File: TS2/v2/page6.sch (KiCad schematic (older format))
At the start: 4 parts

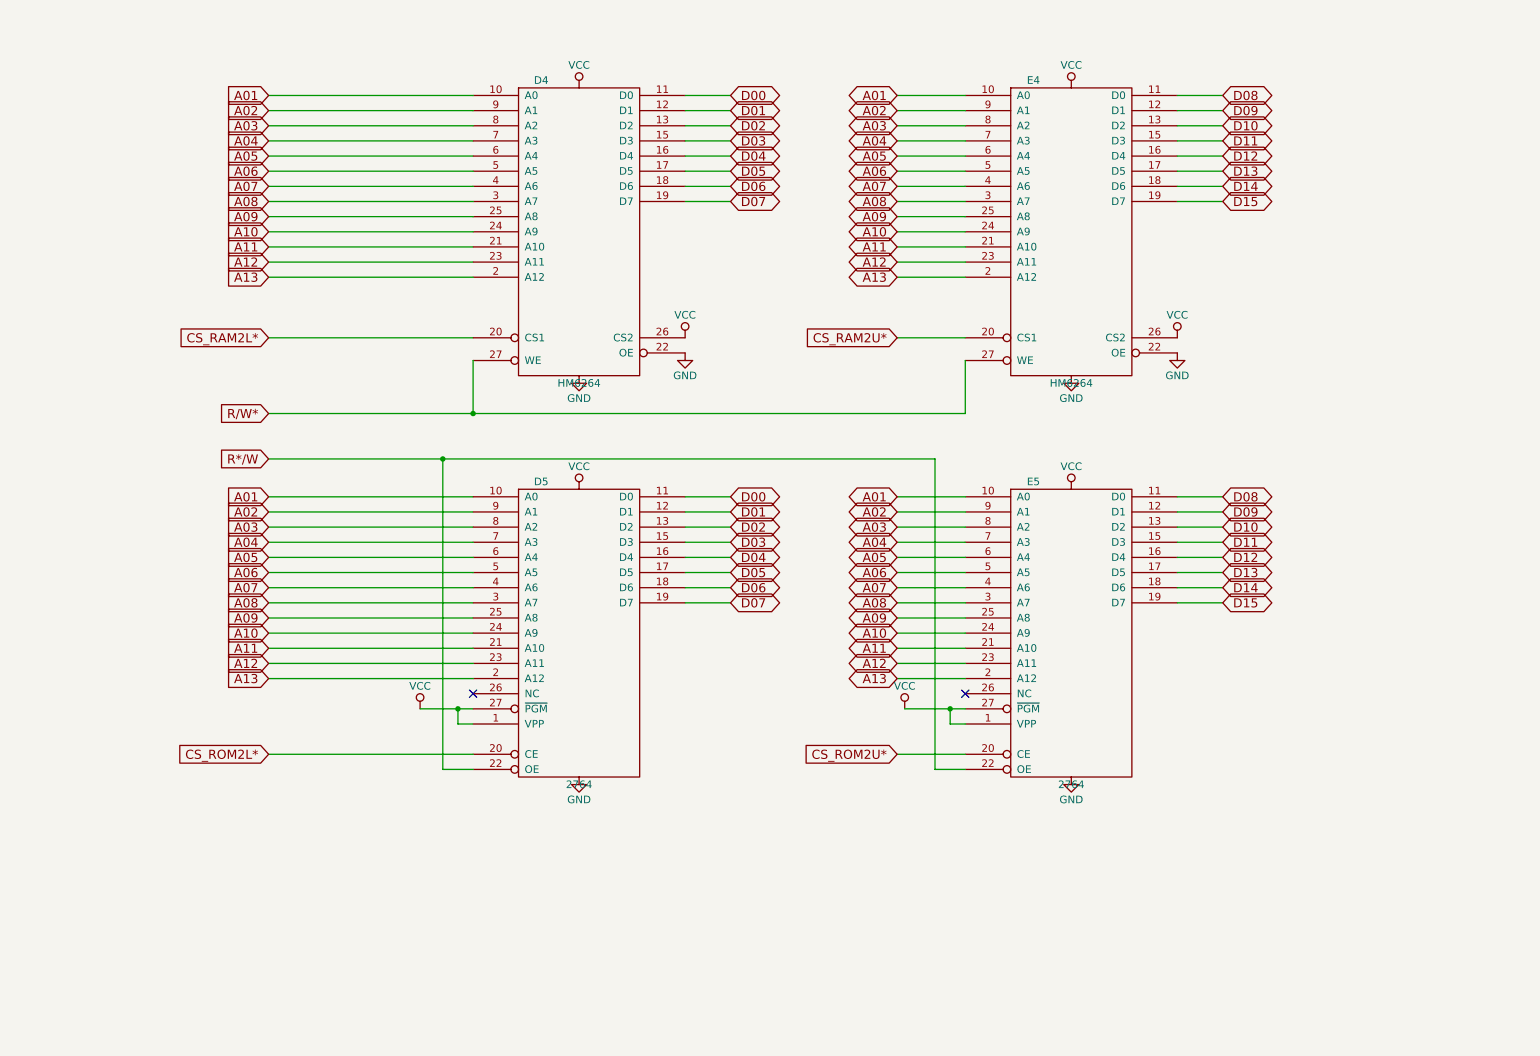
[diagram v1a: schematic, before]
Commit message: more fixup of deleted pages.
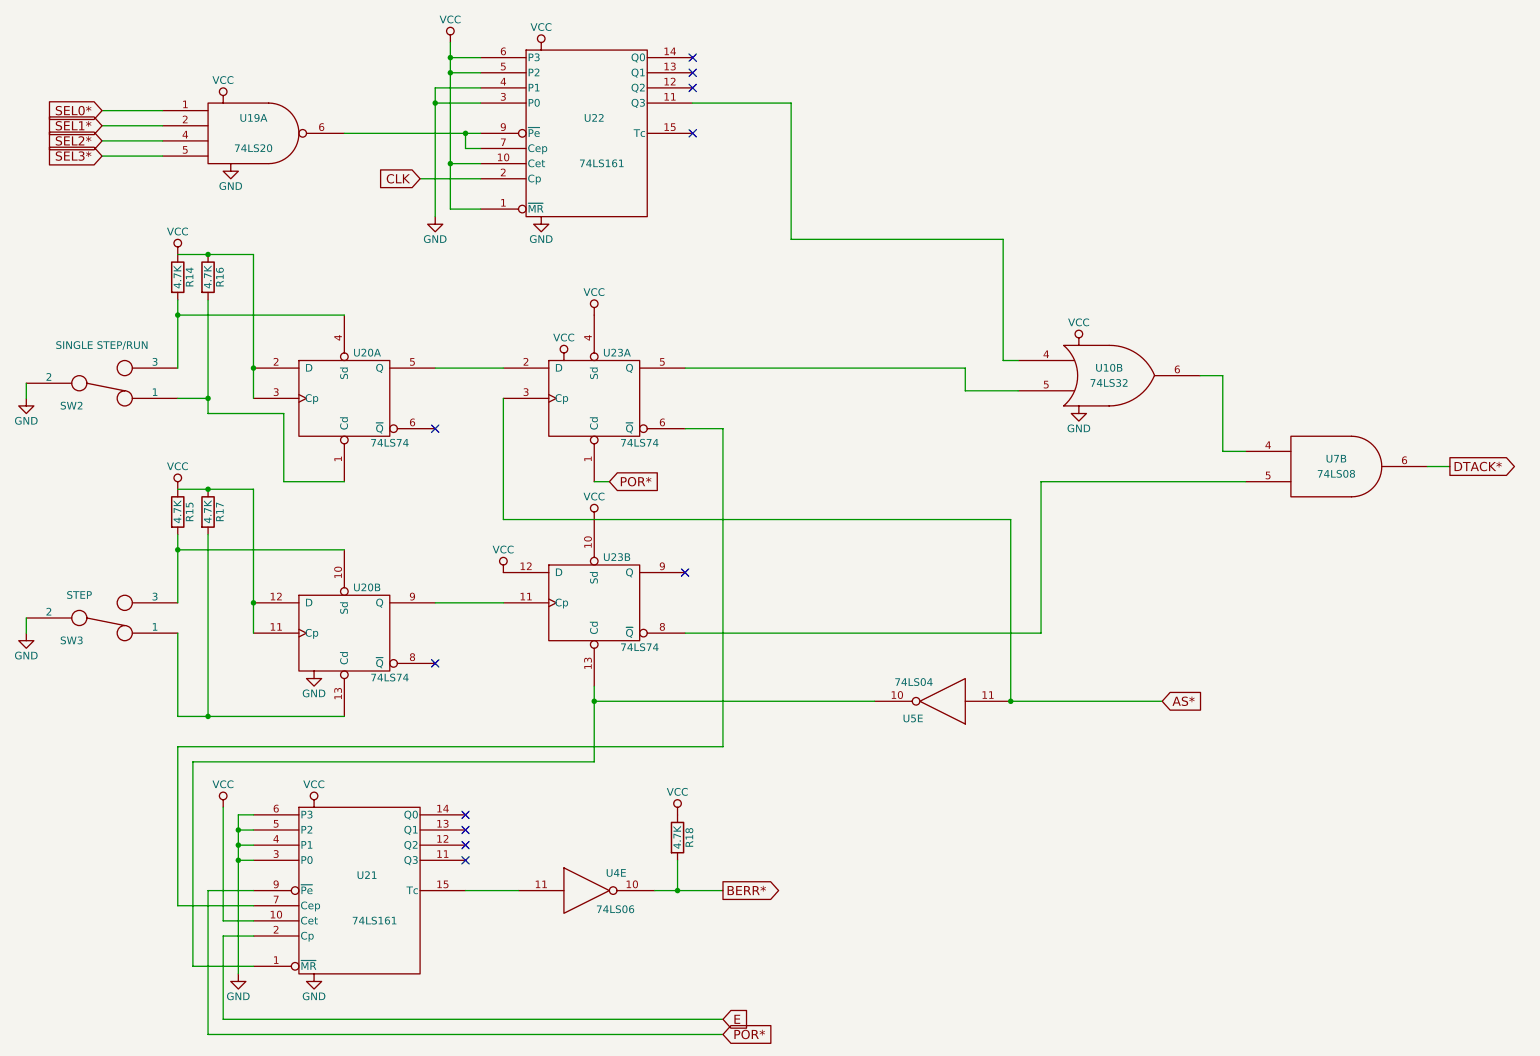
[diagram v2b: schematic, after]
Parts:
- removed D4, E4: HM6264, symbol HM6264
- removed D5, E5: 2764, symbol 2764
- added R14, R15, R16, R17, R18: 4.7K, symbol R
- added SW2: SINGLE STEP/RUN, symbol SWITCH_INV
- added SW3: STEP, symbol SWITCH_INV
- added U10: 74LS32, symbol 74LS32
- added U19: 74LS20, symbol 74LS20
- added U20, U23: 74LS74, symbol 74LS74
- added U21, U22: 74LS161, symbol 74LS161
- added U4: 74LS06, symbol 74LS06
- added U5: 74LS04, symbol 74LS04
- added U7: 74LS08, symbol 74LS08
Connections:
- net GND: now also SW2.2, SW3.2, U10.7 (GND), U19.7 (GND), U20.7 (GND), U20.7 (GND), U21.3 (P0), U21.4 (P1), U21.5 (P2), U21.6 (P3), U21.8 (GND), U22.3 (P0), U22.4 (P1), U22.8 (GND), U23.7 (GND), U23.7 (GND), U4.7 (GND), U5.7 (GND), U7.7 (GND)
- net VCC: now also R14.1, R15.1, R16.1, R17.1, R18.1, U10.14 (VCC), U19.14 (VCC), U20.11 (Cp), U20.12 (D), U20.14 (VCC), U20.14 (VCC), U20.2 (D), U20.3 (Cp), U21.10 (Cet), U21.16 (VCC), U22.1 (~MR), U22.10 (Cet), U22.16 (VCC), U22.5 (P2), U22.6 (P3), U23.10 (Sd), U23.12 (D), U23.14 (VCC), U23.14 (VCC), U23.4 (Sd), U4.14 (VCC), U5.14 (VCC), U7.14 (VCC)
- new net: U19.6, U22.7 (Cep), U22.9 (~Pe)
- new net: U10.4, U22.11 (Q3)
- new net: U20.5 (Q), U23.2 (D)
- new net: U10.5, U23.5 (Q)
- new net: U21.7 (Cep), U23.6 (~Q)
- new net: R16.2, SW2.1, U20.1 (Cd)
- new net: R14.2, SW2.3, U20.4 (Sd)
- new net: R15.2, SW3.3, U20.10 (Sd)
- new net: R17.2, SW3.1, U20.13 (Cd)
- new net: U20.9 (Q), U23.11 (Cp)
- new net: U21.1 (~MR), U23.13 (Cd), U5.10
- new net: U23.8 (~Q), U7.5
- new net: U21.15 (Tc), U4.11
- new net: U10.6, U7.4
- new net AS*: U23.3 (Cp), U5.11
- new net BERR*: R18.2, U4.10
- new net CLK: U22.2 (Cp)
- new net DTACK*: U7.6
- new net E: U21.2 (Cp)
- new net POR*: U21.9 (~Pe), U23.1 (Cd)
- new net SEL0*: U19.1
- new net SEL1*: U19.2
- new net SEL2*: U19.4
- new net SEL3*: U19.5
- no-connect marks 2 -> 11
